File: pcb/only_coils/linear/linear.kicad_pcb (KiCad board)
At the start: 4 copper layers, 100 x 100 mm, 0 parts

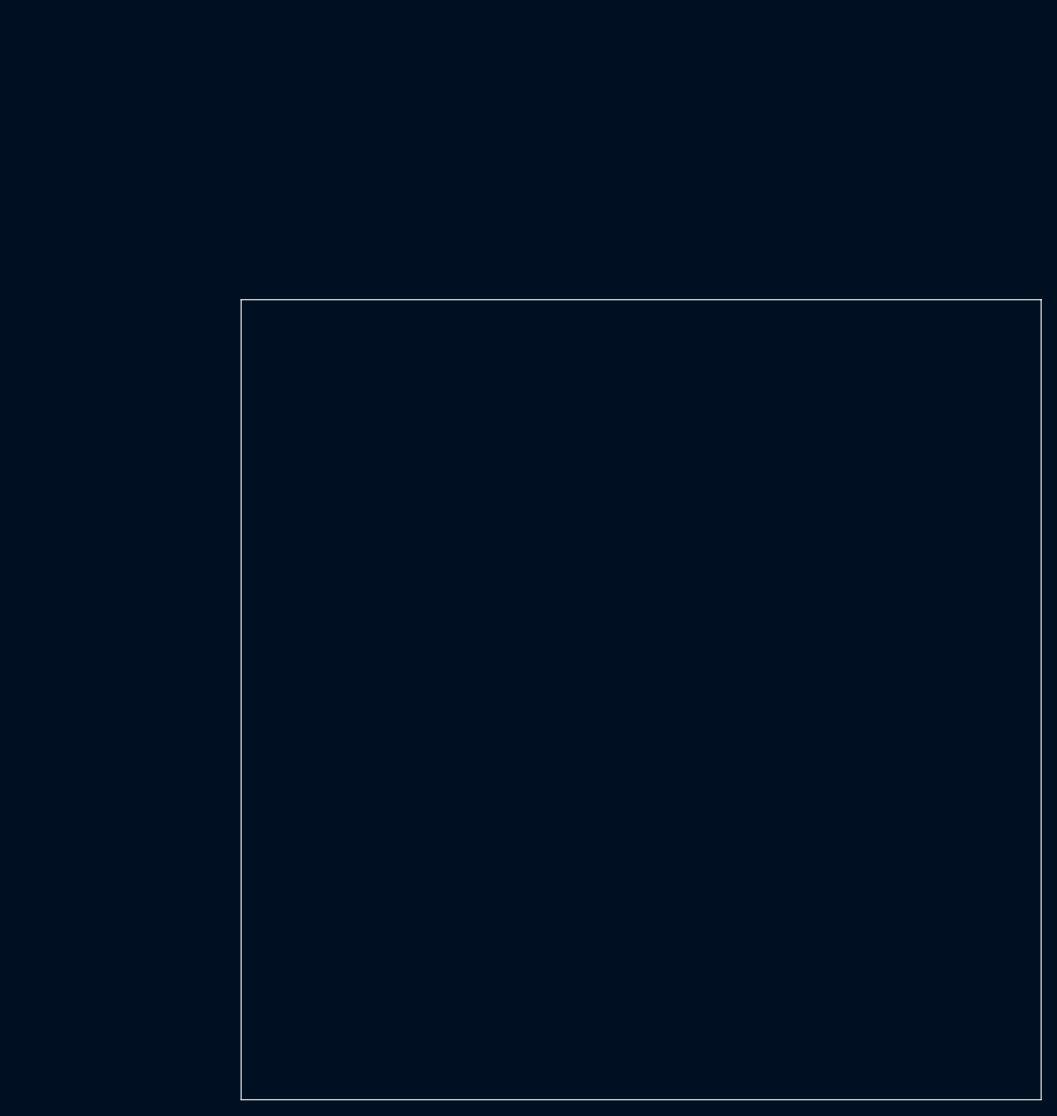
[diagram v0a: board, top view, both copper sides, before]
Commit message: Added small script for square coils
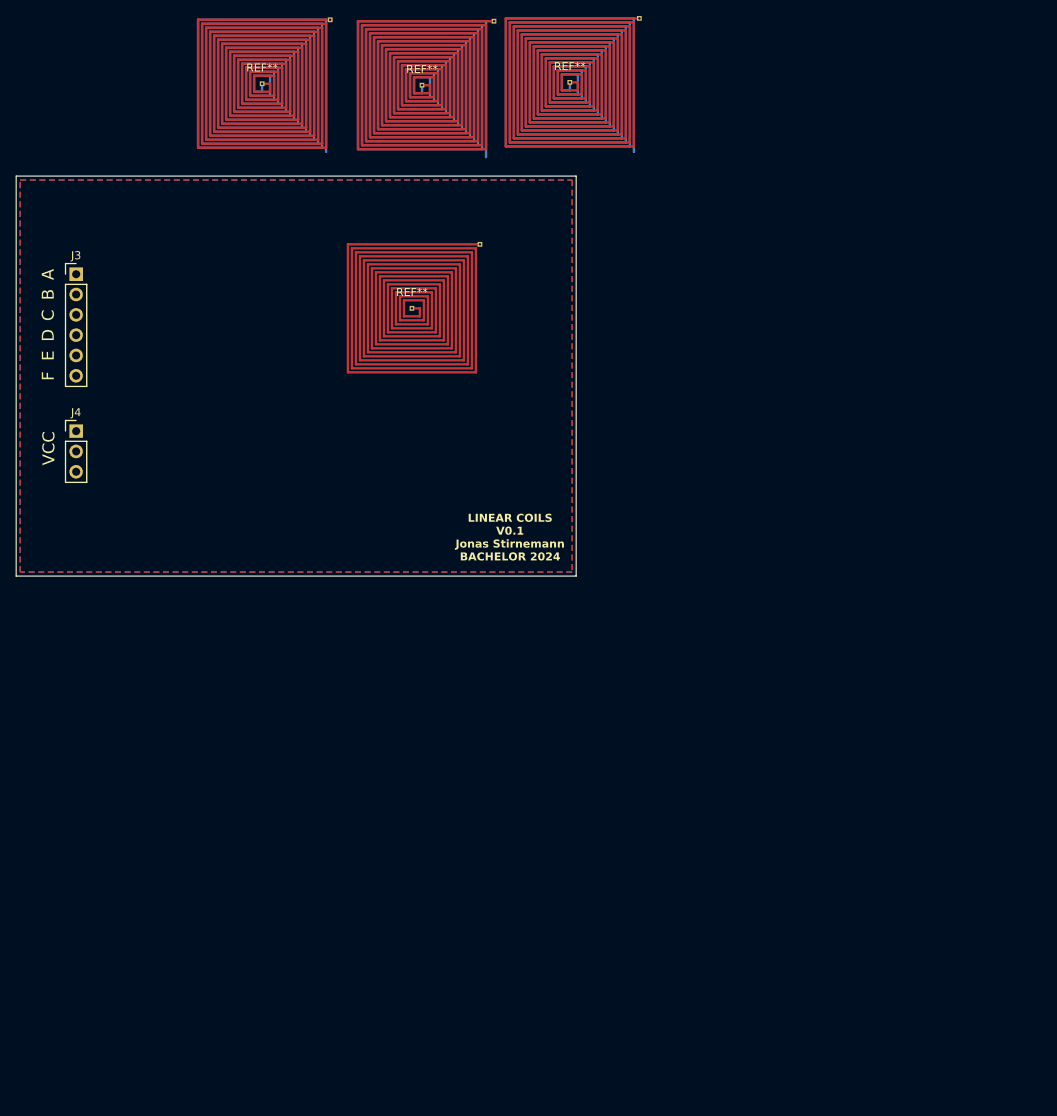
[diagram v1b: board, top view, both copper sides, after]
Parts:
- added J3: Conn_01x06_Pin, Connector_PinHeader_2.54mm:PinHeader_1x06_P2.54mm_Vertical, F.Cu at (79.4, 46.8)
- added J4: Conn_01x03_Pin, Connector_PinHeader_2.54mm:PinHeader_1x03_P2.54mm_Vertical, F.Cu at (79.4, 66.4)
- added REF**: TEST, TEST, F.Cu at (121.3, 51.1)
- added REF**: TEST, TEST, F.Cu at (141.1, 22.8)
- added REF**: TEST, TEST, F.Cu at (102.6, 23.0)
- added REF**: TEST, TEST, F.Cu at (122.6, 23.2)
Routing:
- added copper zone on B.Cu, net (none)
- added copper zone on F.Cu, net (none)
- added copper zone on In1.Cu, net (none)
- added copper zone on In2.Cu, net (none)
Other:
- board size 100 x 100 mm -> 70 x 50 mm
- board text added: "A"
- board text added: "B"
- board text added: "C"
- board text added: "D"
- board text added: "E"
- board text added: "F"
- board text added: "LINEAR COILS V0.1 Jonas Stirnemann BACHELOR 2024"
- board text added: "VCC"

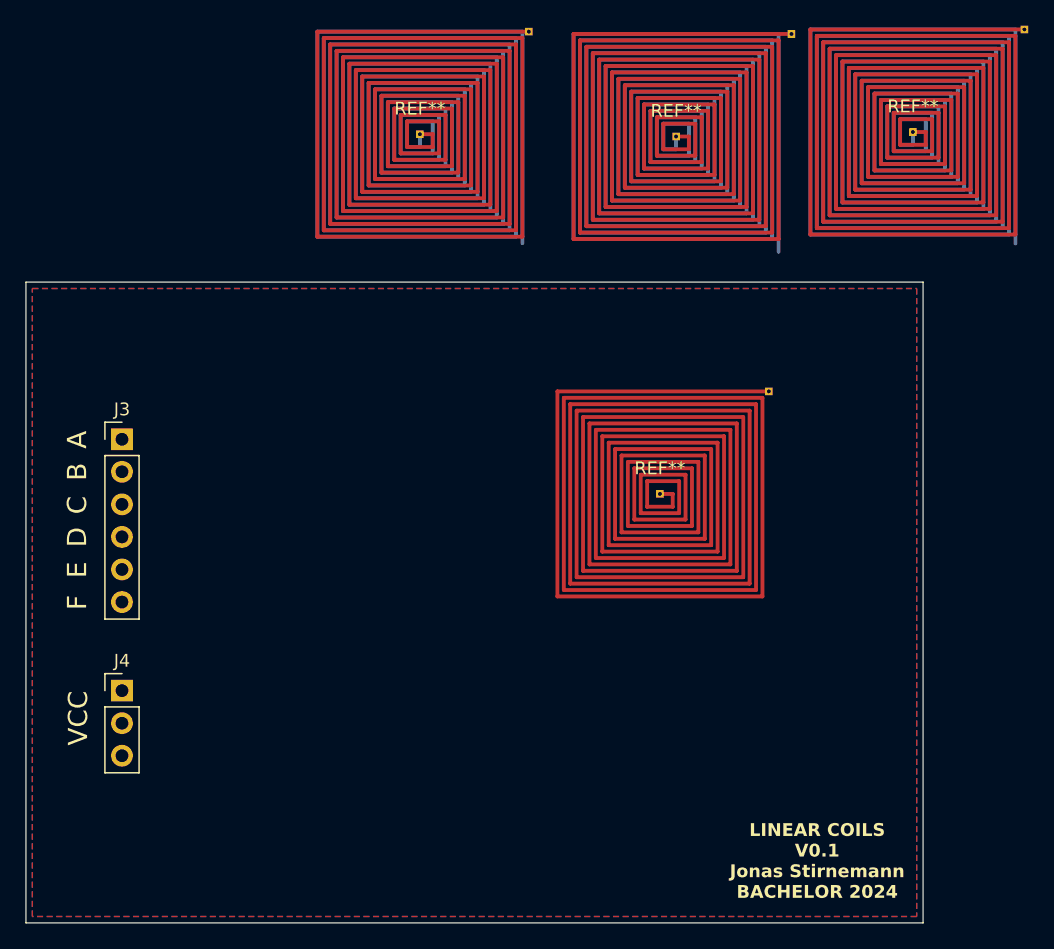
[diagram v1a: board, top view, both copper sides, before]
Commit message: Added finished linear coils PCB
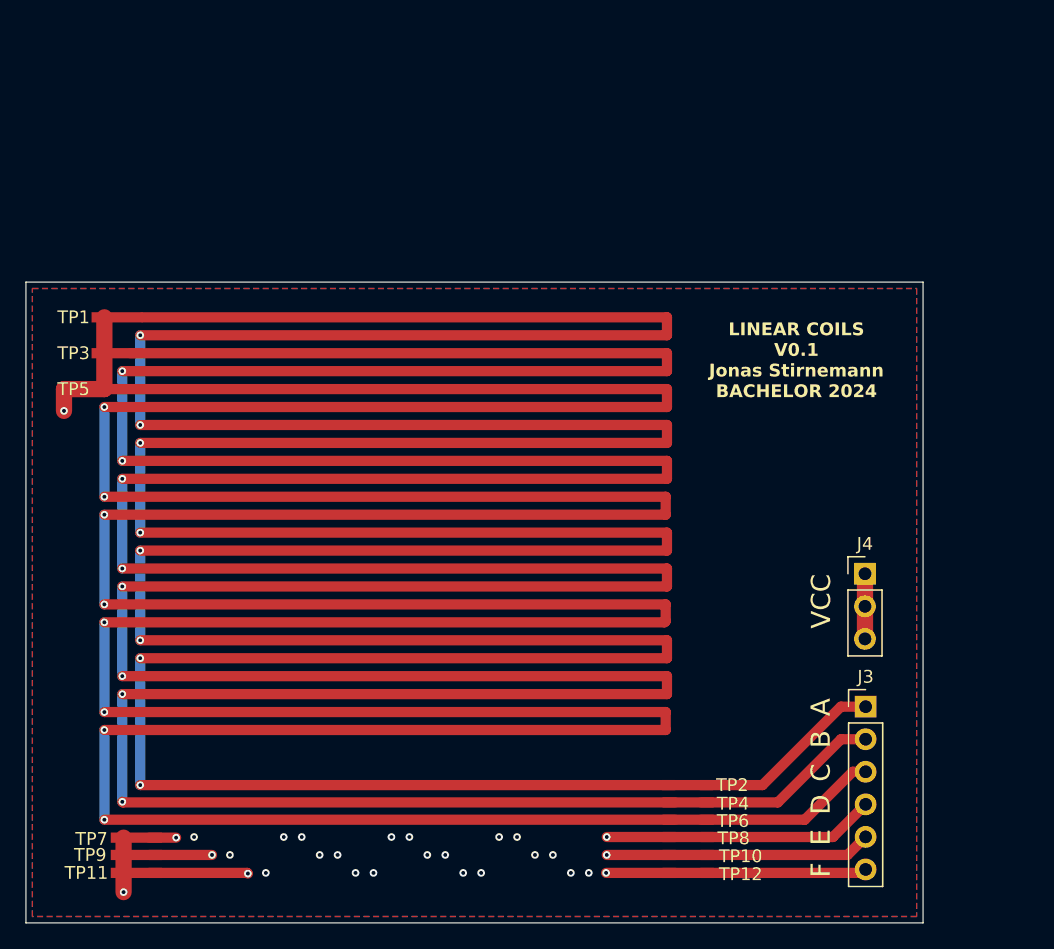
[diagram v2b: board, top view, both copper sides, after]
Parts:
- removed REF** (x4): TEST, TEST
- added TP1: TestPoint_2Pole, pads_dual:pads_dual, F.Cu at (79.0, 37.3)
- added TP10: TestPoint_2Pole, pads_dual:pads_dual, F.Cu at (123.5, 79.2)
- added TP11: TestPoint_2Pole, pads_dual:pads_dual, F.Cu at (80.5, 80.7)
- added TP12: TestPoint_2Pole, pads_dual:pads_dual, F.Cu at (123.5, 80.7)
- added TP2: TestPoint_2Pole, pads_dual:pads_dual, F.Cu at (123.5, 73.8)
- added TP3: TestPoint_2Pole, pads_dual:pads_dual, F.Cu at (79.0, 40.1)
- added TP4: TestPoint_2Pole, pads_dual:pads_dual, F.Cu at (123.5, 75.2)
- added TP5: TestPoint_2Pole, pads_dual:pads_dual, F.Cu at (79.0, 42.9)
- added TP6: TestPoint_2Pole, pads_dual:pads_dual, F.Cu at (123.5, 76.5)
- added TP7: TestPoint_2Pole, pads_dual:pads_dual, F.Cu at (80.5, 77.9)
- added TP8: TestPoint_2Pole, pads_dual:pads_dual, F.Cu at (123.5, 77.8)
- added TP9: TestPoint_2Pole, pads_dual:pads_dual, F.Cu at (80.5, 79.2)
- moved J3 61.7 mm to (137.4, 67.7)
- moved J4 58.7 mm to (137.3, 57.3)
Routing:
- net /COIL_C: track 0.00 -> 425.7 mm, vias 0 -> 8
- net /COIL_B: track 0.00 -> 417.6 mm, vias 0 -> 8
- net /COIL_A: track 0.00 -> 406.8 mm, vias 0 -> 8
- net /COIL_F: track 0.00 -> 391.7 mm, vias 0 -> 9
- net /COIL_E: track 0.00 -> 381.1 mm, vias 0 -> 9
- net /COIL_D: track 0.00 -> 369.9 mm, vias 0 -> 9
- net VCC: track 0.00 -> 19.8 mm, vias 0 -> 2
- net /A: track 0.00 -> 15.4 mm
- net /B: track 0.00 -> 14.9 mm
- net /C: track 0.00 -> 14.4 mm
- net /D: track 0.00 -> 13.9 mm
- net /E: track 0.00 -> 13.4 mm
- net /F: track 0.00 -> 13.0 mm
- added copper zone on B.Cu, net VCC
- added copper zone on F.Cu, net VCC
- added copper zone on In1.Cu, net VCC
- added copper zone on In2.Cu, net VCC
- removed copper zone on B.Cu, net (none)
- removed copper zone on F.Cu, net (none)
- removed copper zone on In1.Cu, net (none)
- removed copper zone on In2.Cu, net (none)
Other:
- board text added: "LINEAR COILS MODULE - 3x signals double lines - 0.8mm width - 0.6mm spacing"
